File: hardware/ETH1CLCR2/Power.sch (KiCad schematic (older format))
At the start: 31 parts, among them Q1101 IRFR5410, U1101 NCP1117-3.3_SOT223, U1102 NMK2405SAC, U1103 NCP1117-5.0_SOT223, U1104 NMK2409SAC, U1106 MAX5902, U1107 NCP1117-5.0_SOT223, U1108 NMK2409SC, U1109 LT1175-5_SOT223

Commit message: Footprints assigned.
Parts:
- added TP901: TestPoint, TestPoint:TestPoint_Plated_Hole_D2.0mm, symbol Connector:TestPoint
- C901: renamed from C1101; footprint (none) -> Capacitor_SMD:C_1206_3216Metric_Pad1.33x1.80mm_HandSolder
- C902: renamed from C1102; footprint (none) -> Capacitor_SMD:C_1206_3216Metric_Pad1.33x1.80mm_HandSolder
- C903: renamed from C919; footprint (none) -> Capacitor_SMD:C_1206_3216Metric_Pad1.33x1.80mm_HandSolder
- C904: renamed from C920; footprint (none) -> Capacitor_SMD:C_1206_3216Metric_Pad1.33x1.80mm_HandSolder
- C905: renamed from C1103; footprint (none) -> Capacitor_SMD:C_1206_3216Metric_Pad1.33x1.80mm_HandSolder
- C906: renamed from C1104; footprint (none) -> Capacitor_SMD:C_1206_3216Metric_Pad1.33x1.80mm_HandSolder
- C907: renamed from C921; footprint (none) -> Capacitor_SMD:C_1206_3216Metric_Pad1.33x1.80mm_HandSolder
- C908: renamed from C922; footprint (none) -> Capacitor_SMD:C_1206_3216Metric_Pad1.33x1.80mm_HandSolder
- C909: renamed from C1107; footprint (none) -> Capacitor_SMD:C_1206_3216Metric_Pad1.33x1.80mm_HandSolder
- C910: renamed from C1108; footprint (none) -> Capacitor_SMD:C_1206_3216Metric_Pad1.33x1.80mm_HandSolder
- C911: renamed from C1111; footprint (none) -> Capacitor_SMD:C_1206_3216Metric_Pad1.33x1.80mm_HandSolder
- C912: renamed from C1112; footprint (none) -> Capacitor_SMD:C_1206_3216Metric_Pad1.33x1.80mm_HandSolder
- C913: renamed from C1109; footprint (none) -> Capacitor_SMD:C_1206_3216Metric_Pad1.33x1.80mm_HandSolder
- C914: renamed from C1110; footprint (none) -> Capacitor_SMD:C_1206_3216Metric_Pad1.33x1.80mm_HandSolder
- C915: renamed from C1113; footprint (none) -> Capacitor_SMD:C_1206_3216Metric_Pad1.33x1.80mm_HandSolder
- C916: renamed from C1114; footprint (none) -> Capacitor_SMD:C_1206_3216Metric_Pad1.33x1.80mm_HandSolder
- D901: renamed from D1101; footprint (none) -> Diode_SMD:D_SOD-123
- D902: renamed from D1102; footprint (none) -> ETH1CLCR2:DO_214AA_REV
- D903: renamed from D1103; footprint (none) -> LED_SMD:LED_0603_1608Metric_Pad1.05x0.95mm_HandSolder
- F901: renamed from F1101; footprint (none) -> ETH1CLCR2:Fuse_SMD2920
- Q901: renamed from Q1101; footprint (none) -> ETH1CLCR2:TO-252-2_Rectifier
- R901: renamed from R1101; footprint (none) -> Resistor_SMD:R_0603_1608Metric_Pad0.98x0.95mm_HandSolder
- R902: renamed from R1102; footprint (none) -> Resistor_SMD:R_0603_1608Metric_Pad0.98x0.95mm_HandSolder
- U902: renamed from U1102; footprint (none) -> ETH1CLCR2:NMK_SINGLE
- U903: renamed from U1106; footprint (none) -> Package_TO_SOT_SMD:SOT-23-6_Handsoldering
- U905: renamed from U1104; footprint (none) -> ETH1CLCR2:NMK_SINGLE
- U907: renamed from U1108; footprint (none) -> ETH1CLCR2:NMK_DUAL
- renumbered U1101 to U901, U1103 to U904, U1107 to U906, U1109 to U908
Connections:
- net GND: now also TP901.1

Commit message: PCB layout
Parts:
- added C905, C906: 4u7/50V, Capacitor_SMD:C_1206_3216Metric_Pad1.33x1.80mm_HandSolder, symbol Device:C
- renumbered C905 to C907, C906 to C908, C907 to C909, C908 to C910, C909 to C911, C910 to C912, C911 to C913, C912 to C914, C913 to C915, C914 to C916, C915 to C917, C916 to C918
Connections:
- net GNDPWR: now also C905.2, C906.2
- net at D901.1 (K), Q901.2 (D), U902.1 (+VIN)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: now also C905.1, C906.1
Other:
- moved on the sheet: C901, C902, C903, C904, C907, C908, C909, C910, C911, C912, C913, C914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

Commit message: PCB layout
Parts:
- added C915, C920: 100u, symbol Device:CP
- renumbered C915 to C916, C916 to C917, C917 to C918, C918 to C919
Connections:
- net +5VA: now also C915.1
- net -5VA: now also C920.2
- net GND: now also C915.2, C920.1
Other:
- moved on the sheet: C901, C902, C903, C904, C905, C906, C907, C908, C909, C910, C911, C912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

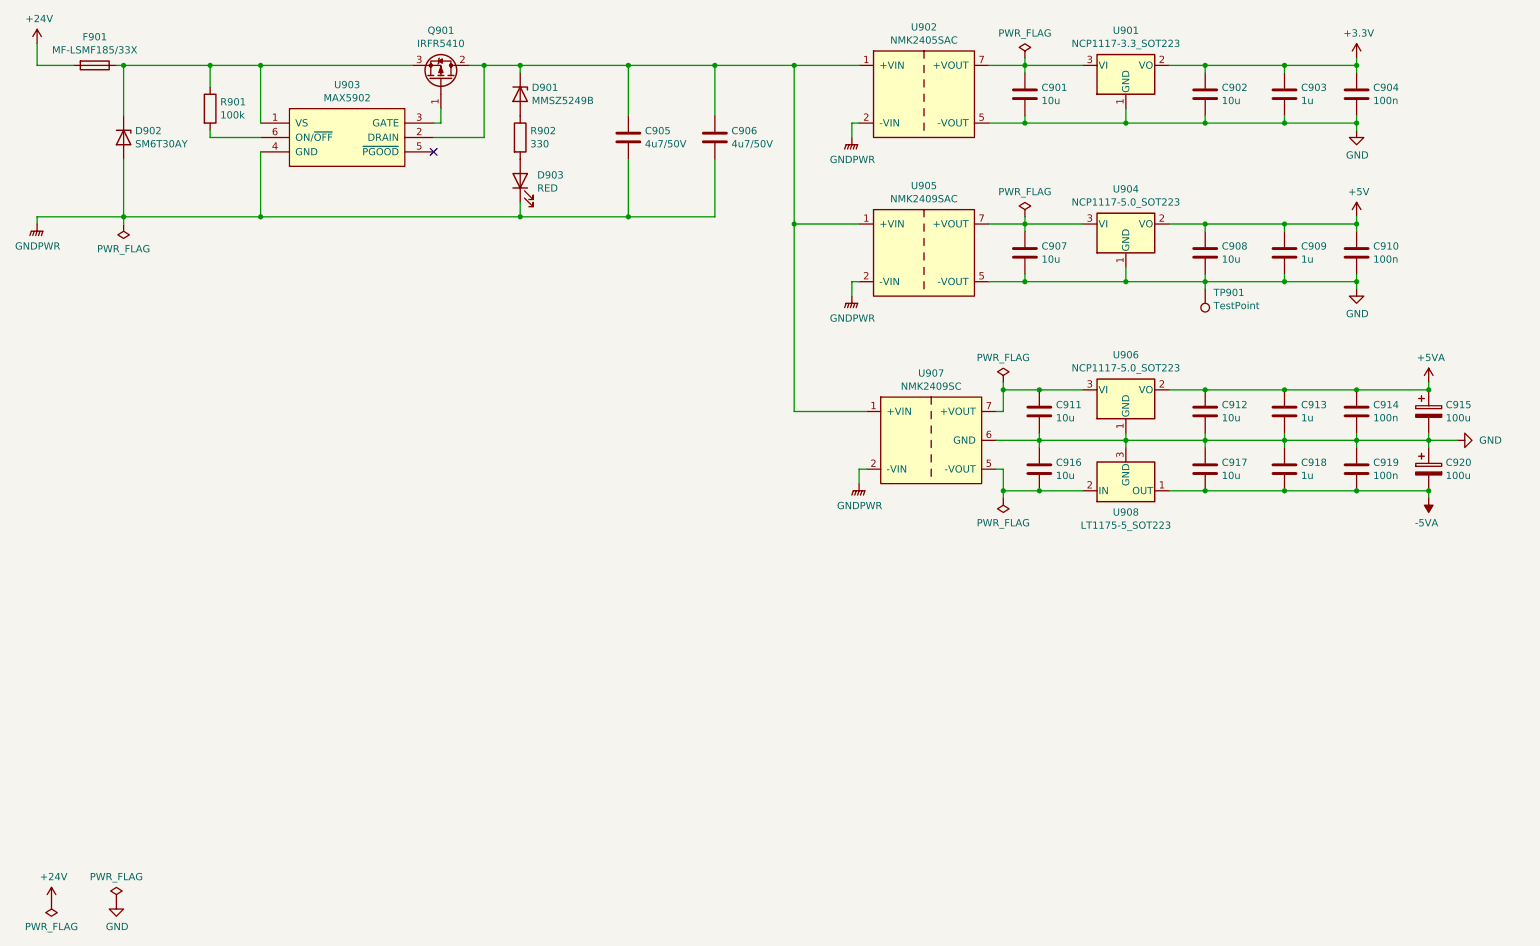
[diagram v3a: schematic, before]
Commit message: Modification of the function generator schematic.
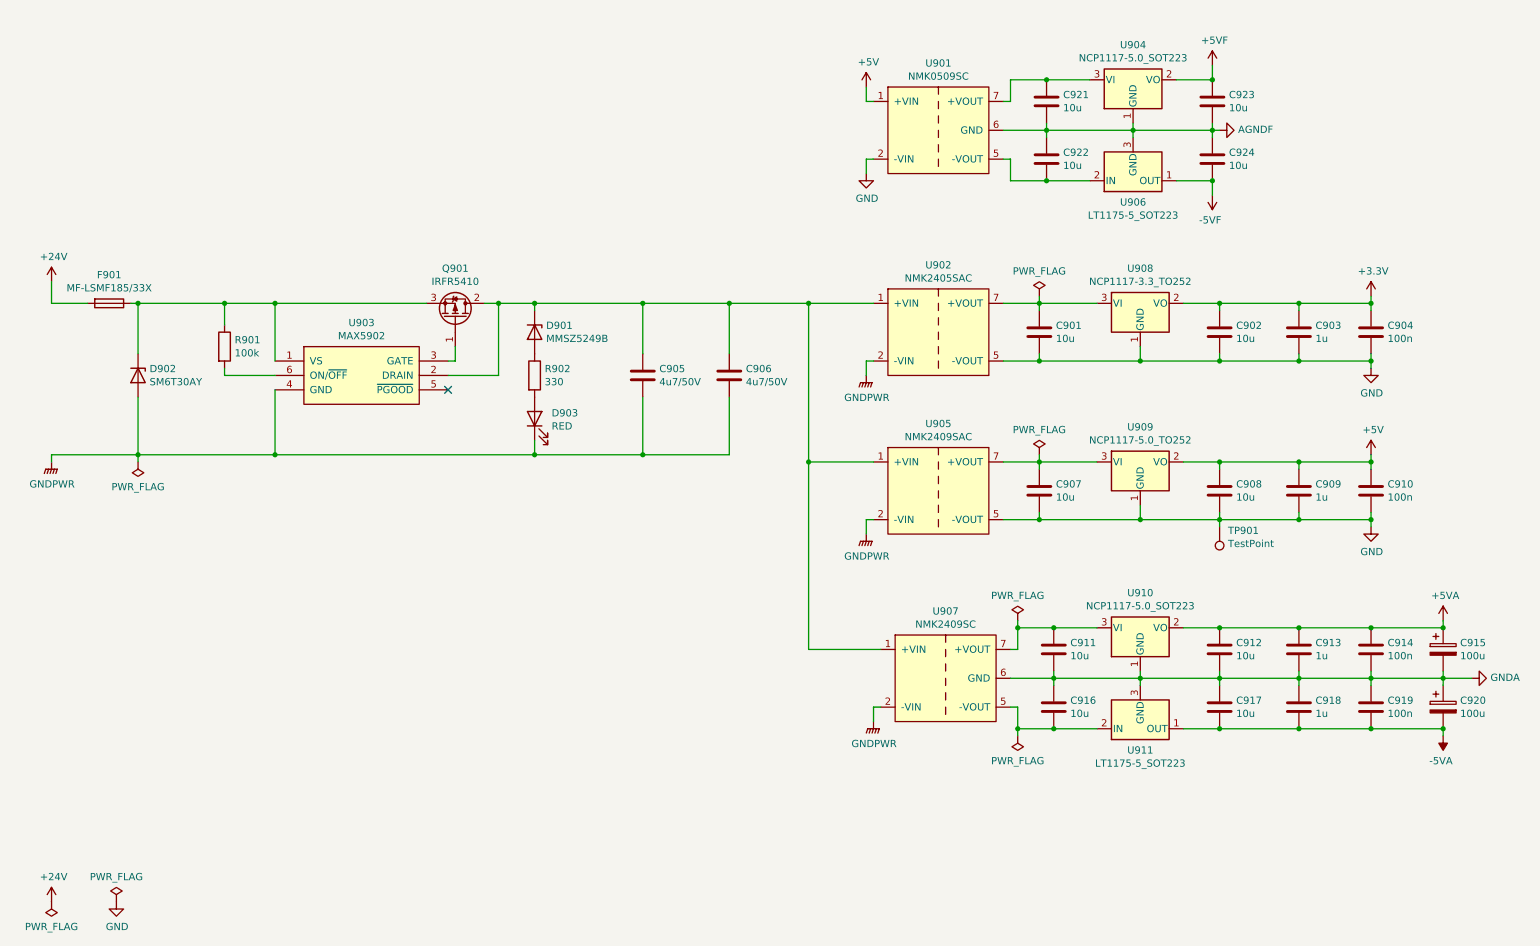
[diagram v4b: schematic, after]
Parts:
- removed U901: NCP1117-3.3_SOT223, Package_TO_SOT_SMD:SOT-223-3_TabPin2, symbol Regulator_Linear:NCP1117-3.3_SOT223
- removed U906: NCP1117-5.0_SOT223, Package_TO_SOT_SMD:SOT-223-3_TabPin2, symbol Regulator_Linear:NCP1117-5.0_SOT223
- removed U908: LT1175-5_SOT223, Package_TO_SOT_SMD:SOT-223-3_TabPin2, symbol Regulator_Linear:LT1175-5_SOT223
- added C921, C922, C923, C924: 10u, Capacitor_SMD:C_1206_3216Metric_Pad1.33x1.80mm_HandSolder, symbol Device:C
- added U901: NMK0509SC, ETH1CLCR2:NMK_DUAL, symbol ETH1CLCR2:NMK_DUAL
- added U906, U911: LT1175-5_SOT223, Package_TO_SOT_SMD:SOT-223-3_TabPin2, symbol Regulator_Linear:LT1175-5_SOT223
- added U908: NCP1117-3.3_TO252, Package_TO_SOT_SMD:TO-252-2, symbol Regulator_Linear:NCP1117-3.3_TO252
- added U909: NCP1117-5.0_TO252, Package_TO_SOT_SMD:TO-252-2, symbol Regulator_Linear:NCP1117-5.0_TO252
- added U910: NCP1117-5.0_SOT223, Package_TO_SOT_SMD:SOT-223-3_TabPin2, symbol Regulator_Linear:NCP1117-5.0_SOT223
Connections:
- net +3V3: now also U908.2 (VO)
- net +5V: now also U901.1 (+VIN), U909.2 (VO); no longer U904.2 (VO)
- net +5VA: now also U910.2 (VO)
- net -5VA: now also U911.1 (OUT)
- net GND: now also U901.2 (-VIN), U908.1 (GND), U909.1 (GND); no longer C911.2, C912.2, C913.2, C914.2, C915.2, C916.1, C917.1, C918.1, C919.1, C920.1, U904.1 (GND), U907.6 (GND)
- net at C901.1, U902.7 (+VOUT): now also U908.3 (VI)
- net at C907.1, U905.7 (+VOUT): now also U909.3 (VI); no longer U904.3 (VI)
- net at C916.2, U907.5 (-VOUT): now also U911.2 (IN)
- net at C911.1, U907.7 (+VOUT): now also U910.3 (VI)
- new net: C922.2, U901.5 (-VOUT), U906.2 (IN)
- new net: C921.1, U901.7 (+VOUT), U904.3 (VI)
- new net +5VF: C923.1, U904.2 (VO)
- new net -5VF: C924.2, U906.1 (OUT)
- new net AGNDF: C921.2, C922.1, C923.2, C924.1, U901.6 (GND), U904.1 (GND), U906.3 (GND)
- new net GNDA: C911.2, C912.2, C913.2, C914.2, C915.2, C916.1, C917.1, C918.1, C919.1, C920.1, U907.6 (GND), U910.1 (GND), U911.3 (GND)
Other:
- moved on the sheet: C901, C902, C903, C904, C905, C906, C907, C908, C909, C910, C911, C912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

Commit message: Schematic
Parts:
- removed C921, C922, C923, C924: 10u, Capacitor_SMD:C_1206_3216Metric_Pad1.33x1.80mm_HandSolder, symbol Device:C
- removed U901: NMK0509SC, ETH1CLCR2:NMK_DUAL, symbol ETH1CLCR2:NMK_DUAL
- removed U902: NMK2405SAC, ETH1CLCR2:NMK_SINGLE, symbol ETH1CLCR2:NMK_SINGLE
- removed U904: NCP1117-5.0_SOT223, Package_TO_SOT_SMD:SOT-223-3_TabPin2, symbol Regulator_Linear:NCP1117-5.0_SOT223
- removed U906: LT1175-5_SOT223, Package_TO_SOT_SMD:SOT-223-3_TabPin2, symbol Regulator_Linear:LT1175-5_SOT223
- added C?: 4u7, symbol Device:C
- added L?: 10u, symbol Device:L
- added U?: NCS3S1205SC, symbol ETH1CLCR2:NCS3
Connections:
- net GND: now also U?.7 (-VOUT)
- net GNDPWR: now also C?.2, U?.1 (-VIN)
- net at C905.1, C906.1, D901.1 (K)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: now also C?.1, L?.1
- net at C901.1, U908.3 (VI): now also U?.6 (+VOUT)
- new net: L?.2, U?.2 (+VIN)
- no-connect marks 1 -> 2
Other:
- moved on the sheet: C901, C902, C903, C904, U908

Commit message: Schematic
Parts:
- C921: renamed from C?; footprint (none) -> Capacitor_SMD:C_1206_3216Metric_Pad1.33x1.80mm_HandSolder
- gave numbers to parts that had none: 2
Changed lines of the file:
@@
 $Descr A4 11693 8268
 encoding utf-8
-Sheet 9 13
+Sheet 9 12
 Title ""
 Date ""
@@
 	8300 3050 8700 3050
 $Comp
-L ETH1CLCR2:NCS3 U?
+L ETH1CLCR2:NCS3 U901
 U 1 1 60B9EE6D
 P 7600 3250
-F 0 "U?" H 7600 3715 50  0000 C CNN
+F 0 "U901" H 7600 3715 50  0000 C CNN
 F 1 "NCS3S1205SC" H 7600 3624 50  0000 C CNN
 F 2 "" H 7600 3250 50  0001 C CNN
@@
 NoConn ~ 7150 3250
 $Comp
-L Device:L L?
+L Device:L L901
 U 1 1 60BCA4CE
 P 6900 3050
-F 0 "L?" V 7090 3050 50  0000 C CNN
+F 0 "L901" V 7090 3050 50  0000 C CNN
 F 1 "10u" V 6999 3050 50  0000 C CNN
 F 2 "" H 6900 3050 50  0001 C CNN
@@
 	7050 3050 7150 3050
 $Comp
-L Device:C C?
+L Device:C C921
 U 1 1 60BCC6E4
 P 6600 3250
-F 0 "C?" H 6715 3296 50  0000 L CNN
+F 0 "C921" H 6715 3296 50  0000 L CNN
 F 1 "4u7" H 6715 3205 50  0000 L CNN
-F 2 "" H 6638 3100 50  0001 C CNN
+F 2 "Capacitor_SMD:C_1206_3216Metric_Pad1.33x1.80mm_HandSolder" H 6638 3100 50  0001 C CNN
 F 3 "~" H 6600 3250 50  0001 C CNN
 	1    6600 3250

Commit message: Footprints
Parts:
- removed U908: NCP1117-3.3_TO252, Package_TO_SOT_SMD:TO-252-2, symbol Regulator_Linear:NCP1117-3.3_TO252
- removed U909: NCP1117-5.0_TO252, Package_TO_SOT_SMD:TO-252-2, symbol Regulator_Linear:NCP1117-5.0_TO252
- removed U910: NCP1117-5.0_SOT223, Package_TO_SOT_SMD:SOT-223-3_TabPin2, symbol Regulator_Linear:NCP1117-5.0_SOT223
- removed U911: LT1175-5_SOT223, Package_TO_SOT_SMD:SOT-223-3_TabPin2, symbol Regulator_Linear:LT1175-5_SOT223
- added U902: TLV1117-33, Package_TO_SOT_SMD:TO-263-3_TabPin2, symbol Regulator_Linear:TLV1117-33
- added U904, U906: TLV1117-50, Package_TO_SOT_SMD:TO-263-3_TabPin2, symbol Regulator_Linear:TLV1117-50
- added U908: LM2990SX-5.0, Package_TO_SOT_SMD:TO-263-3_TabPin2, symbol Regulator_Linear:LM2990SX-5.0
- C915, C920: value 100u -> T521V107M016ATE050; footprint (none) -> Capacitor_Tantalum_SMD:CP_EIA-7343-20_Kemet-V_Pad2.25x2.55mm_HandSolder
- L901: value 10u -> PM1608S-100M-RC; footprint (none) -> ETH1CLCR2:PM1608S
- U901: footprint (none) -> ETH1CLCR2:NCS3
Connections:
- net +3V3: now also U902.2 (VO)
- net +5V: now also U904.2 (VO)
- net +5VA: now also U906.2 (VO)
- net -5VA: now also U908.3 (OUT)
- net GND: now also U902.1 (GND), U904.1 (GND)
- net GNDA: now also U906.1 (GND), U908.1 (GND)
- net at C907.1, U905.7 (+VOUT): now also U904.3 (VI)
- net at C916.2, U907.5 (-VOUT): now also U908.2 (IN)
- net at C911.1, U907.7 (+VOUT): now also U906.3 (VI)
- net at C901.1, U901.6 (+VOUT): now also U902.3 (VI)
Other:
- moved on the sheet: C911, C912, C913, C914, C915, C916, C917, C918, C919, C920, C921, L901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
